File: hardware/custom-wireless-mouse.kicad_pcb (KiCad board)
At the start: 2 copper layers, 0 parts

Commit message: Fix 3D model orientation for U1, SW1, SW2-5, and ENC1
All four footprints' vendor/community STEP models were placed with
identity (model ...) transforms that didn't match their own internal
axis conventions, causing them to render sheared, rotated, or flipped
relative to their pads. Diagnosed by parsing each STEP file's
CARTESIAN_POINT bounding box and iteratively verifying fixes with
`kicad-cli pcb render`:

- U1 (Nordic QFN) and SW1 (C&K slide switch): both STEP files use a
  Y-up axis convention instead of KiCad's Z-up. Fixed with a -90
  rotation about X on each.
- SW2-5 (Omron D2FC, 4 instances): STEP model's long axis and origin
  didn't match the footprint's local frame. Fixed with a 90 rotation
  about Z plus a corrective offset.
- ENC1 (TTC/Kailh encoder): best-effort fix only. A 90 rotation about
  Y produces a mechanically plausible orientation (flat body, shaft
  horizontal) but pin-to-pad registration couldn't be fully verified
  against this already-unconfirmed placeholder footprint — documented
  plainly in that library's ATTRIBUTION.md rather than overstated.

Fixes applied to both the source .kicad_mod library files and the
already-placed instances embedded in the .kicad_pcb (PCB footprint
instances carry their own copy of the model transform, independent of
the library file). DRC re-run clean (0 violations) after all edits.
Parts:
- added C1: 100nF, Capacitor_SMD:C_0603_1608Metric, F.Cu at (151.2, 98.0)
- added C10: 100nF, Capacitor_SMD:C_0603_1608Metric, F.Cu at (155.3, 114.7)
- added C11: 1uF, Capacitor_SMD:C_0603_1608Metric, F.Cu at (153.3, 114.7)
- added C12: 10uF, Capacitor_SMD:C_0603_1608Metric, F.Cu at (155.3, 125.7)
- added C13: 10nF, Capacitor_SMD:C_0603_1608Metric, F.Cu at (153.3, 125.7)
- added C14: 100nF, Capacitor_SMD:C_0603_1608Metric, F.Cu at (153.3, 118.7)
- added C15: 10uF, Capacitor_SMD:C_0603_1608Metric, F.Cu at (136.0, 102.9)
- added C16: 10uF, Capacitor_SMD:C_0603_1608Metric, F.Cu at (146.0, 101.9)
- added C2: 100nF, Capacitor_SMD:C_0603_1608Metric, F.Cu at (161.5, 98.8)
- added C3: 100nF, Capacitor_SMD:C_0603_1608Metric, F.Cu at (161.5, 100.5)
- added C4: 100nF, Capacitor_SMD:C_0603_1608Metric, F.Cu at (156.2, 94.8)
- added C5: 1uF, Capacitor_SMD:C_0603_1608Metric, F.Cu at (155.0, 104.8)
- added C6: 12pF NP0, Capacitor_SMD:C_0402_1005Metric, F.Cu at (160.4, 96.2)
- added C7: 12pF NP0, Capacitor_SMD:C_0402_1005Metric, F.Cu at (164.9, 96.2)
- added C8: 10uF, Capacitor_SMD:C_0603_1608Metric, F.Cu at (136.3, 118.7)
- added C9: 100nF, Capacitor_SMD:C_0603_1608Metric, F.Cu at (134.3, 118.7)
- added ENC1: MOUSE_ENCODER, ttc-kailh-mouse-encoder:encoder-tht-placeholder-mouse-wheel, F.Cu at (128.5, 87.7)
- added F1: 0603L010, littelfuse-0603l010:fuse-0603-littelfuse-0603l010, F.Cu at (126.2, 117.0)
- added J1: SWD_HEADER, samtec-tsw-104-07-t-s:pinheader-1x04-p2.54mm-vertical, F.Cu at (159.2, 107.0)
- added J2: B2B-XH-A, jst-b2b-xh-a:battery-conn-jst-b2b-xh-a, F.Cu at (126.5, 122.0)
- added L1: 4.7uH, Inductor_SMD:L_1008_2520Metric, F.Cu at (140.0, 96.9)
- added Q1: DMG2305UXQ, diodes-dmg2305uxq:sot-23-dmg2305uxq, F.Cu at (127.0, 113.0)
- added R1: 10k, Resistor_SMD:R_0603_1608Metric, F.Cu at (136.3, 122.7)
- added R2: 499k, Resistor_SMD:R_0603_1608Metric, F.Cu at (144.0, 101.9)
- added R3: 180k, Resistor_SMD:R_0603_1608Metric, F.Cu at (145.0, 104.9)
- added SW1: JS202011SCQN, ck-js202011scqn:switch-slide-js202011scqn, F.Cu at (128.0, 105.0)
- added SW2: D2FC-F-7N(20M), omron-d2fc-f-7n:switch-tht-omron-d2fc-f-7n, F.Cu at (127.0, 68.0)
- added SW3: D2FC-F-7N(20M), omron-d2fc-f-7n:switch-tht-omron-d2fc-f-7n, F.Cu at (163.0, 68.1)
- added SW4: D2FC-F-7N(20M), omron-d2fc-f-7n:switch-tht-omron-d2fc-f-7n, F.Cu at (145.0, 86.0)
- added SW5: D2FC-F-7N(20M), omron-d2fc-f-7n:switch-tht-omron-d2fc-f-7n, F.Cu at (150.0, 68.1)
- added U1: nRF52810-QCAA-T, nordic-nrf52810-qcxx:qfn-32-1ep-5x5mm-p0.5mm-ep3.6x3.6mm, F.Cu at (156.6, 99.8)
- added U2: PMW3610DM-SUDU, pmw3610dm-sudu:pmw3610dm-sudu-16-pin, F.Cu at (145.0, 118.0)
- added U3: TLV61220DBVT, ti-tlv61220:sot-23-6, F.Cu at (139.9, 101.0)
- added Y1: NX2016SA-32MHZ, ndk-nx2016sa:crystal-smd-2016-4pin-2.0x1.6mm, F.Cu at (162.8, 96.2)
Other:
- board outline added: 50 x 70 mm

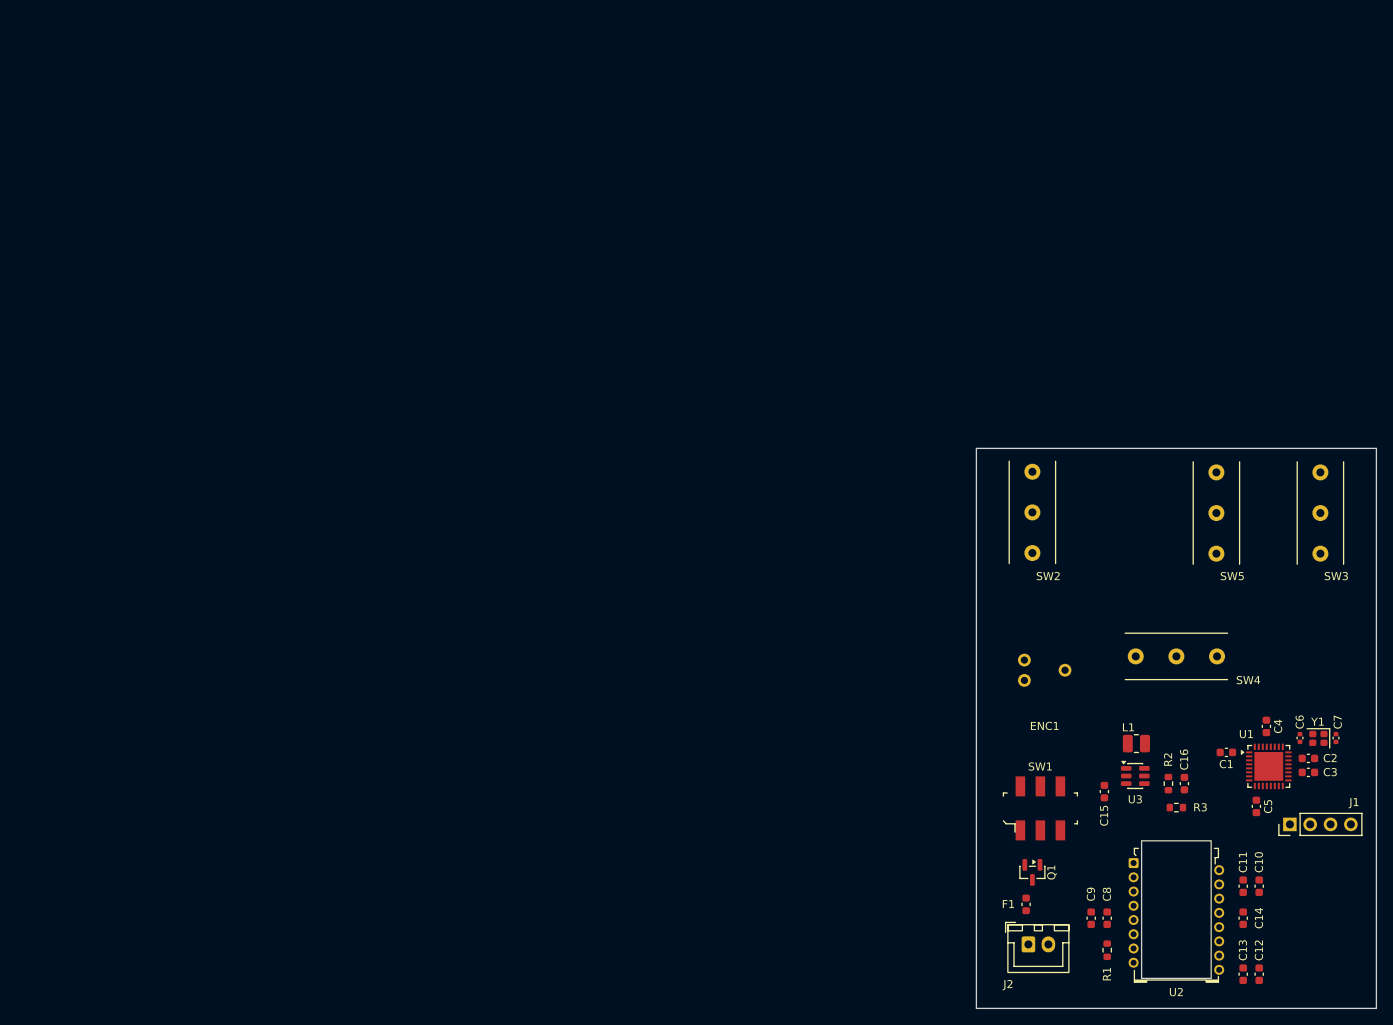
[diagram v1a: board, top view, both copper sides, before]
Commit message: Sync ENC1 and PMW3610 footprints from library after 3D model tweaks
Re-ran the footprint-library sync (identical mechanism as the earlier
U1/SW1/SW2-5/ENC1 orientation fixes) to bring two manually-tweaked
vendored footprints into the placed PCB instances: ENC1's refined
encoder model transform and added mounting pads, and U2/PMW3610's
adjusted sensor rotation. Position, orientation, custom sourcing
fields, and net connections were all preserved during the sync;
DRC re-confirmed clean afterward.
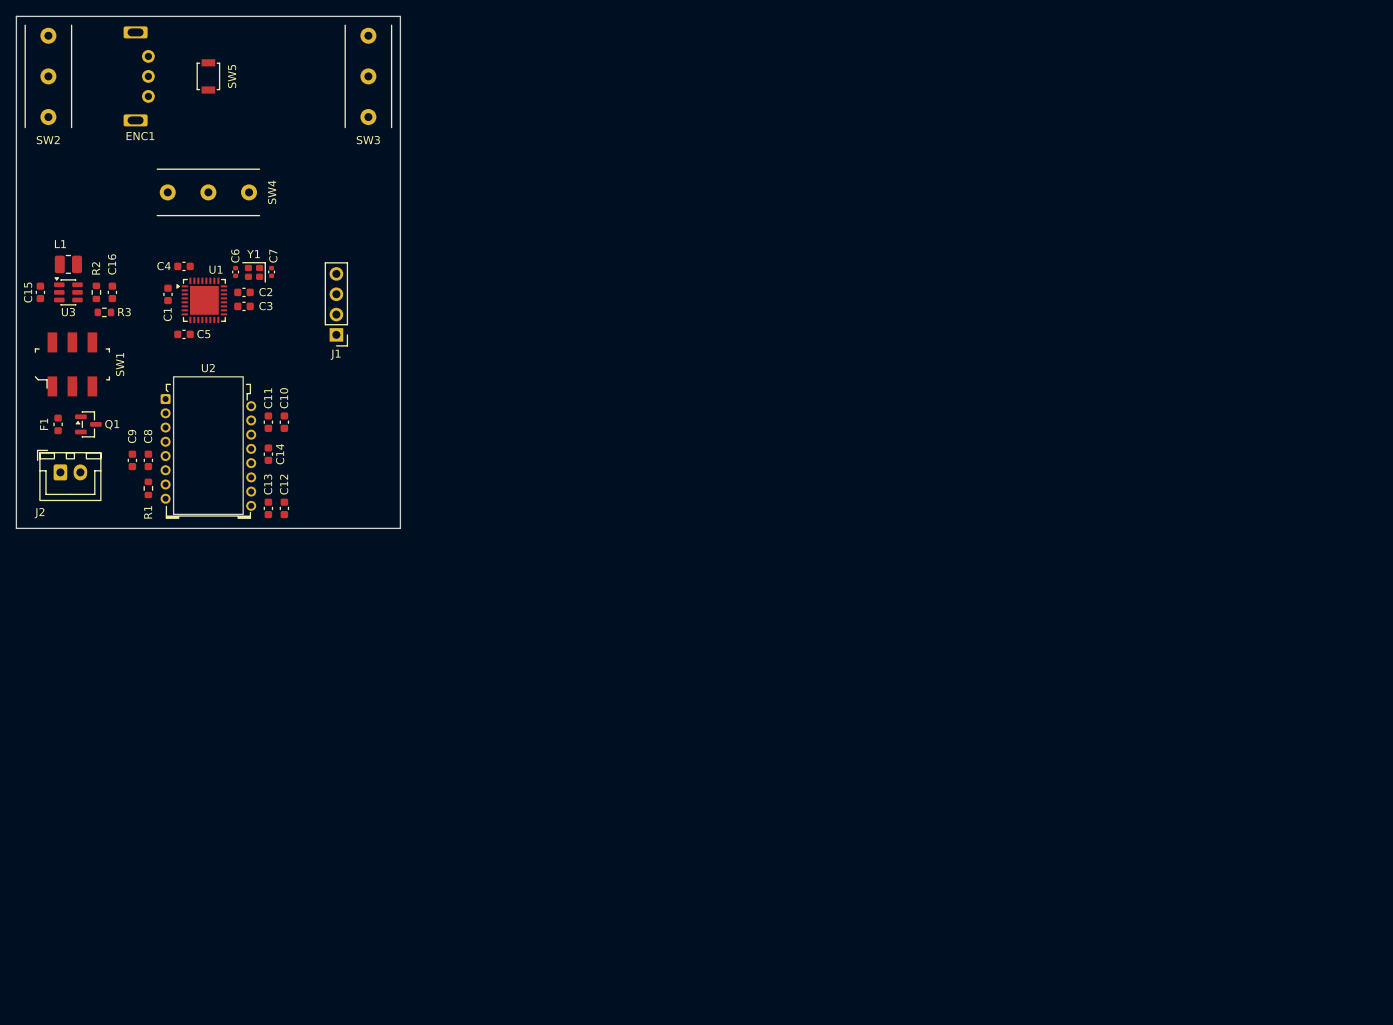
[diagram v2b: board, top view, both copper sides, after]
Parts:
- SW5: value D2FC-F-7N(20M) -> B3U-1000P; footprint omron-d2fc-f-7n:switch-tht-omron-d2fc-f-7n -> omron-b3u-1000p:switch-smd-omron-b3u-1000p
- moved R3 147.6 mm to (11.0, 43.0)
- moved C16 147.4 mm to (12.0, 40.5)
- moved R2 147.4 mm to (10.0, 40.5)
- moved C4 147.0 mm to (20.9, 37.2), turned to 180 degrees
- moved C15 146.9 mm to (3.00, 40.5), turned to 90 degrees
- moved C5 146.5 mm to (20.9, 45.8), turned to 180 degrees
- moved U3 146.4 mm to (6.50, 40.5)
- moved L1 146.3 mm to (6.50, 37.0)
- moved C2 145.2 mm to (28.4, 40.5)
- moved C3 145.2 mm to (28.4, 42.2)
- moved U1 145.2 mm to (23.5, 41.5)
- moved Y1 145.2 mm to (29.7, 38.0)
- moved C6 145.2 mm to (27.4, 38.0)
- moved C7 145.2 mm to (31.9, 38.0)
- moved C1 144.2 mm to (18.9, 40.8), turned to -90 degrees
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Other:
- board size 50 x 70 mm -> 48 x 64 mm
